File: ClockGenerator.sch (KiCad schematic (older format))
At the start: 6 parts, among them IC1 LTC6903CMS8#PBF, U4 74AHC273

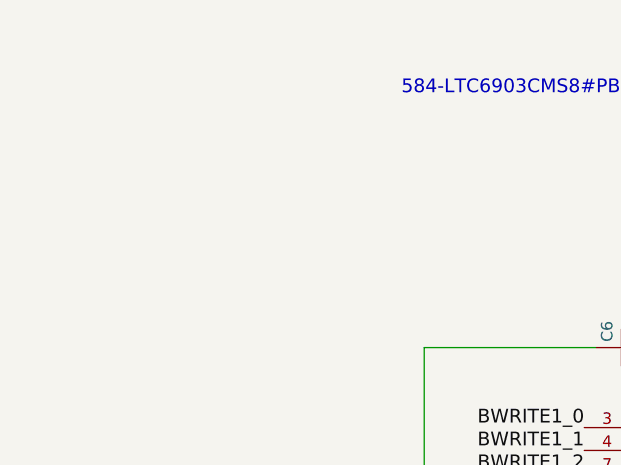
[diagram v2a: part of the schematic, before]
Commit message: adding a potential oscillator
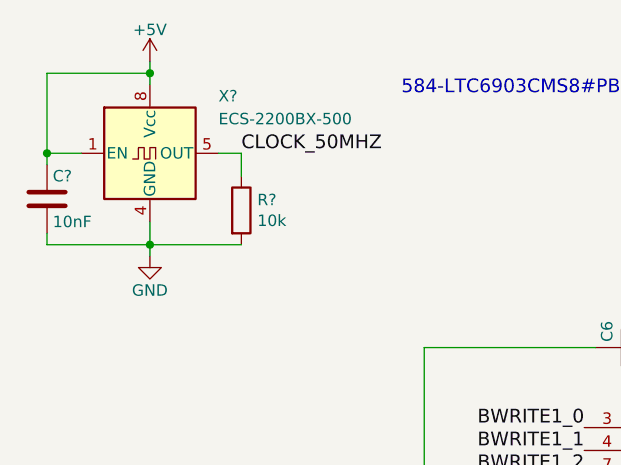
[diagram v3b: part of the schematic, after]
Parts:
- added C?: 10nF, Capacitor_SMD:C_0805_2012Metric, symbol Device:C
- added R?: 10k, symbol Device:R
- added X?: ECS-2200BX-500, Oscillator:Oscillator_DIP-8, symbol Oscillator:CXO_DIP8
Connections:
- net +5V: now also C?.1, X?.1 (EN), X?.8 (Vcc)
- net GND: now also C?.2, R?.2, X?.4 (GND)
- new net CLOCK_50MHZ: R?.1, X?.5 (OUT)
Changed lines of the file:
@@
 NoConn ~ 4350 4100
 NoConn ~ 4350 4200
+$Comp
+L Oscillator:CXO_DIP8 X?
+U 1 1 5F7511AB
+P 1450 2300
+F 0 "X?" H 1750 2550 50  0000 L CNN
+F 1 "ECS-2200BX-500" H 1750 2450 50  0000 L CNN
+F 2 "Oscillator:Oscillator_DIP-8" H 1900 1950 50  0001 C CNN
+F 3 "http://cdn-reichelt.de/documents/datenblatt/B400/OSZI.pdf" H 1350 2300 50  0001 C CNN
+	1    1450 2300
+	1    0    0    -1
+$EndComp
+$Comp
+L power:+5V #PWR?
+U 1 1 5F7518C8
+P 1450 1900
+AR Path="/5F7518C8" Ref="#PWR?"  Part="1"
+AR Path="/5B3313A4/5F7518C8" Ref="#PWR?"  Part="1"
+F 0 "#PWR?" H 1450 1750 50  0001 C CNN
+F 1 "+5V" H 1450 2040 50  0000 C CNN
+F 2 "" H 1450 1900 50  0001 C CNN
+F 3 "" H 1450 1900 50  0001 C CNN
+	1    1450 1900
+	1    0    0    -1
+$EndComp
+$Comp
+L power:GND #PWR?
+U 1 1 5F751B8A
+P 1450 2750
+AR Path="/5F751B8A" Ref="#PWR?"  Part="1"
+AR Path="/5B3313A4/5F751B8A" Ref="#PWR?"  Part="1"
+F 0 "#PWR?" H 1450 2500 50  0001 C CNN
+F 1 "GND" H 1450 2600 50  0000 C CNN
+F 2 "" H 1450 2750 50  0001 C CNN
+F 3 "" H 1450 2750 50  0001 C CNN
+	1    1450 2750
+	1    0    0    -1
+$EndComp
+$Comp
+L Device:C C?
+U 1 1 5F751FC7
+P 1000 2500
+AR Path="/5F751FC7" Ref="C?"  Part="1"
+AR Path="/5B3313A4/5F751FC7" Ref="C?"  Part="1"
+F 0 "C?" H 1025 2600 50  0000 L CNN
+F 1 "10nF" H 1025 2400 50  0000 L CNN
+F 2 "Capacitor_SMD:C_0805_2012Metric" H 1038 2350 50  0001 C CNN
+F 3 "" H 1000 2500 50  0001 C CNN
+	1    1000 2500
+	1    0    0    -1
+$EndComp
+Text Label 1850 2300 0    60   ~ 0
+CLOCK_50MHZ
+Wire Wire Line
+	1450 1900 1450 1950
+Wire Wire Line
+	1450 2600 1450 2700
+$Comp
+L Device:R R?
+U 1 1 5F754723
+P 1850 2550
+F 0 "R?" H 1920 2596 50  0000 L CNN
+F 1 "10k" H 1920 2505 50  0000 L CNN
+F 2 "" V 1780 2550 50  0001 C CNN
+F 3 "~" H 1850 2550 50  0001 C CNN
+	1    1850 2550
+	1    0    0    -1
+$EndComp
+Wire Wire Line
+	1850 2700 1450 2700
+Wire Wire Line
+	1450 2700 1450 2750
+Connection ~ 1450 2700
+Wire Wire Line
+	1850 2400 1850 2300
+Wire Wire Line
+	1850 2300 1750 2300
+Connection ~ 1450 1950
+Wire Wire Line
+	1450 1950 1450 2000
+Wire Wire Line
+	1000 1950 1000 2300
+Wire Wire Line
+	1000 1950 1450 1950
+Wire Wire Line
+	1150 2300 1000 2300
+Connection ~ 1000 2300
+Wire Wire Line
+	1000 2300 1000 2350
+Wire Wire Line
+	1000 2650 1000 2700
+Wire Wire Line
+	1000 2700 1450 2700
 Wire Bus Line
 	1900 6350 1900 7150
